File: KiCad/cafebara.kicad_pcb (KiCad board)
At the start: 4 copper layers, 49 x 32 mm, 60 parts, among them J1 Micro_SD_Card_Det2, J2 USB_C_Receptacle_USB2.0_14P, J3 PROG, J4 Conn_01x19_MountingPin, J6 EDID, Q1 NMOS, SW1 SW_Push, U3 ATtiny1616-M, U4 M24C02-RMC, U5 BQ25895RTW

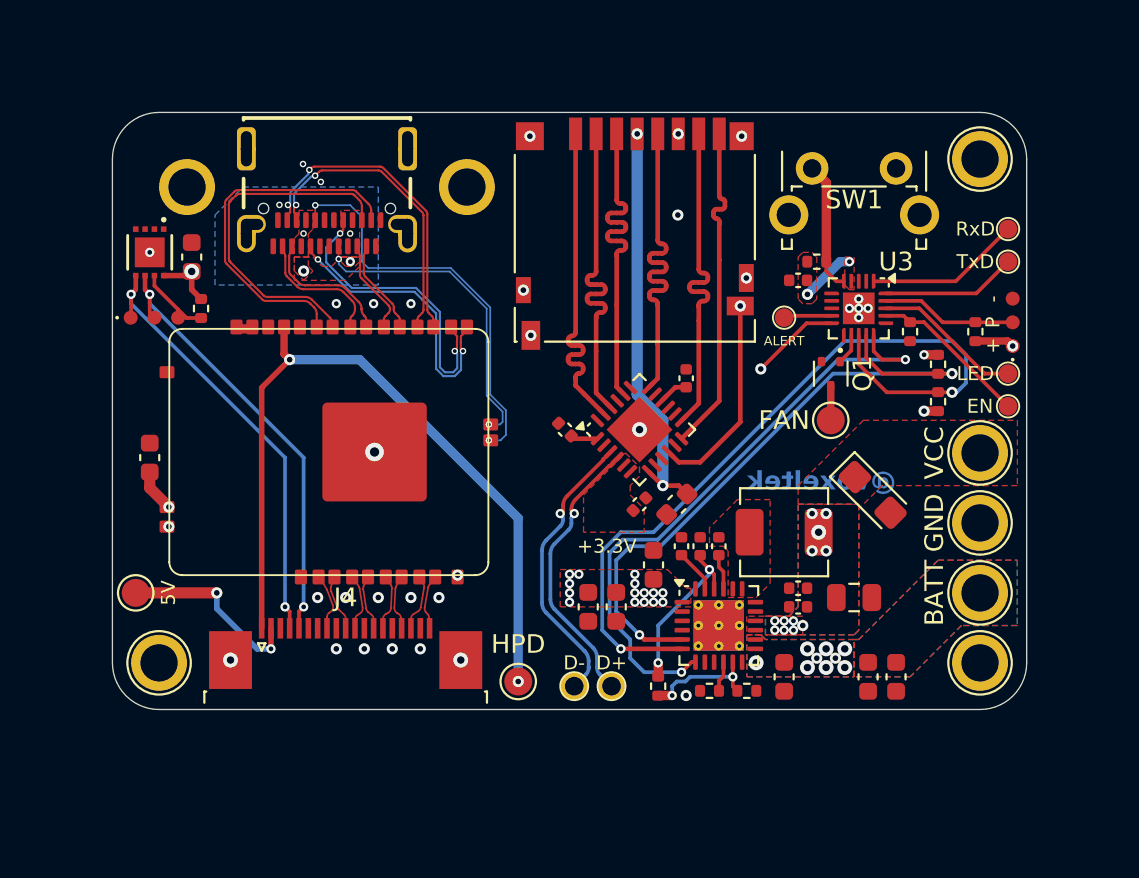
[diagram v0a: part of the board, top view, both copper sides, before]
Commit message: Begin change to new battery charge IC
TODO:
- complete transition
- add battery protection
- add fuel gauge?
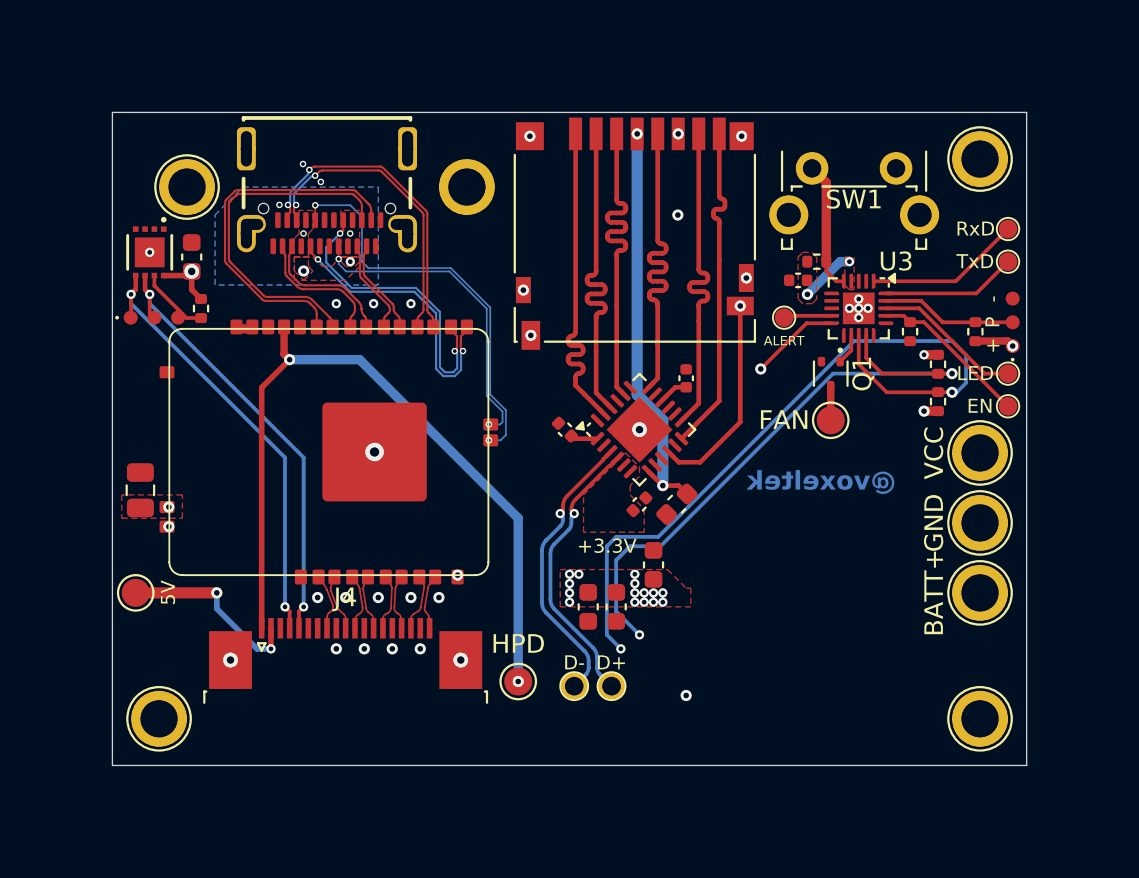
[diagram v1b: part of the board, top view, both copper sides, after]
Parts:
- removed C11: 22uF, Capacitor_SMD:C_0805_2012Metric
- removed C12: 47nF, Capacitor_SMD:C_0402_1005Metric
- removed C13, C16, C20: 10uF, Capacitor_SMD:C_0603_1608Metric
- removed C14: 4.7uF, Capacitor_SMD:C_0402_1005Metric
- removed C17, C18, C8: 22uF, Capacitor_SMD:C_0402_1005Metric
- removed C19: 100uF, Capacitor_Tantalum_SMD:CP_EIA-3216-10_Kemet-I
- removed L1: 3.3uH, Inductor_SMD:L_APV_APH0420
- removed R6: 260, Resistor_SMD:R_0402_1005Metric
- removed R7: 5.23k, Resistor_SMD:R_0402_1005Metric
- removed R8: 30.1k, Resistor_SMD:R_0402_1005Metric
- removed U5: BQ25895RTW, Package_DFN_QFN:Texas_RTW_WQFN-24-1EP_4x4mm_P0.5mm_EP2.7x2.7mm_ThermalVias
- C1: footprint Capacitor_SMD:C_0603_1608Metric -> Capacitor_SMD:C_0805_2012Metric
- TP5: value BATT -> BATT+
- moved H1 3.00 mm to (68.2, 74.0)
- moved H3 3.00 mm to (112.2, 74.0), turned to 90 degrees
- moved C1 1.82 mm to (67.2, 61.8)
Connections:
- TP5 pad 1: /BATT -> /BATT+
- U3 pad 15: ~{BQ_INT} -> unconnected-(U3-PC0-Pad15)
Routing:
- net ~{BQ_INT}: track 33.0 -> 0.00 mm, vias 2 -> 0
- net Net-(U5-REGN): track 9.00 -> 0.00 mm, vias 2 -> 0
- net Net-(U5-TS): track 6.33 -> 0.00 mm, vias 2 -> 0
- net SDA: track 43.1 -> 39.6 mm
- net SCL: track 35.2 -> 32.8 mm
- net Net-(U5-PMID): track 2.33 -> 0.00 mm
- net VBUS: track 20.1 -> 17.8 mm
- net Net-(U5-BTST): track 1.91 -> 0.00 mm
- net Net-(U5-ILIM): track 1.64 -> 0.00 mm
- net VCC: vias 17 -> 5
- net /BATT: vias 9 -> 0
- removed copper zone on B.Cu, net /BATT
- removed copper zone on F.Cu, net /BATT
- removed copper zone on In2.Cu, net /BATT
- removed copper zone on F.Cu, net Net-(C12-Pad1)
- removed copper zone on B.Cu, net VCC
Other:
- board size 49 x 32 mm -> 49 x 35 mm

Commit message: More misc progress
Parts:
- added REF**: Vishay_PowerPAK_SC70-6L_Single, Package_TO_SOT_SMD:Vishay_PowerPAK_SC70-6L_Single, F.Cu at (138.2, 79.3)
- added REF**: Diodes_UDFN2020-6_Type-F, Package_DFN_QFN:Diodes_UDFN2020-6_Type-F, F.Cu at (134.7, 79.3)
- added REF**: Vishay_PowerPAK_1212-8_Single, Package_SO:Vishay_PowerPAK_1212-8_Single, F.Cu at (153.0, 74.0)

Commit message: More misc work
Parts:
- removed the REF** at (138.2, 79.3)
- removed the REF** at (134.7, 79.3)
- removed the REF** at (153.0, 74.0)
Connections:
- net /BATT+ renamed /BMS/BATT+

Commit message: More work for BMS portion
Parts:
- added C11: 100uF, Capacitor_Tantalum_SMD:CP_EIA-3216-10_Kemet-I, F.Cu at (109.1, 93.2)
- added C12: 47nF, Capacitor_SMD:C_0402_1005Metric, F.Cu at (104.0, 65.5)
- added C13: 47nF, Capacitor_SMD:C_0402_1005Metric, F.Cu at (104.0, 107.5)
- added C14: 10nF, Capacitor_SMD:C_0402_1005Metric, F.Cu at (104.0, 109.5)
- added C16: 10nF, Capacitor_SMD:C_0402_1005Metric, F.Cu at (104.0, 111.5)
- added C17: 22uF, Capacitor_SMD:C_0402_1005Metric, F.Cu at (104.0, 113.5)
- added C18: 22uF, Capacitor_SMD:C_0402_1005Metric, F.Cu at (104.0, 115.4)
- added C19: 100uF, Capacitor_Tantalum_SMD:CP_EIA-3216-10_Kemet-I, F.Cu at (109.1, 96.4)
- added C20: 1nF, Capacitor_SMD:C_0402_1005Metric, F.Cu at (106.8, 103.6)
- added C21: 33nF, Capacitor_SMD:C_0402_1005Metric, F.Cu at (106.8, 105.6)
- added C22: 33nF, Capacitor_SMD:C_0402_1005Metric, F.Cu at (106.8, 107.5)
- added C23: 0.1uF, Capacitor_SMD:C_0402_1005Metric, F.Cu at (106.8, 109.5)
- added C24: 0.1uF, Capacitor_SMD:C_0402_1005Metric, F.Cu at (106.8, 111.5)
- added C25: 1uF, Capacitor_SMD:C_0402_1005Metric, F.Cu at (106.8, 113.5)
- added C26: 10uF, Capacitor_SMD:C_0603_1608Metric, F.Cu at (113.9, 96.2)
- added C27: 10uF, Capacitor_SMD:C_0603_1608Metric, F.Cu at (113.9, 98.7)
- added C28: 3.3uF, Capacitor_SMD:C_0402_1005Metric, F.Cu at (106.8, 115.4)
- added C29: 1uF, Capacitor_SMD:C_0402_1005Metric, F.Cu at (109.7, 103.6)
- added C30: 100pF, Capacitor_SMD:C_0402_1005Metric, F.Cu at (109.7, 105.6)
- added C31: 100pF, Capacitor_SMD:C_0402_1005Metric, F.Cu at (109.7, 107.5)
- added C32: 33pF, Capacitor_SMD:C_0402_1005Metric, F.Cu at (109.7, 109.5)
- added C33: 4.7nF, Capacitor_SMD:C_0402_1005Metric, F.Cu at (109.7, 111.5)
- added C34: 15pF, Capacitor_SMD:C_0402_1005Metric, F.Cu at (109.7, 113.5)
- added C35: 680pF, Capacitor_SMD:C_0402_1005Metric, F.Cu at (109.7, 115.4)
- added C8: 1uF, Capacitor_SMD:C_0402_1005Metric, F.Cu at (104.0, 103.6)
- added L1: 4.7uH, Inductor_SMD:L_APV_APH0420, F.Cu at (106.0, 62.5)
- added Q10: DMT3006, Package_DFN_QFN:Diodes_UDFN2020-6_Type-F, F.Cu at (104.3, 100.9)
- added Q2: DMT3006, Package_DFN_QFN:Diodes_UDFN2020-6_Type-F, F.Cu at (96.0, 93.5)
- added Q3: DMT3006, Package_DFN_QFN:Diodes_UDFN2020-6_Type-F, F.Cu at (96.0, 97.2)
- added Q4: DMT3006, Package_DFN_QFN:Diodes_UDFN2020-6_Type-F, F.Cu at (96.0, 100.9)
- added Q5: DMT3006, Package_DFN_QFN:Diodes_UDFN2020-6_Type-F, F.Cu at (100.1, 93.5)
- added Q6: DMP1009, Package_DFN_QFN:Diodes_UDFN2020-6_Type-F, F.Cu at (100.1, 97.2)
- added Q7: DMT3006, Package_DFN_QFN:Diodes_UDFN2020-6_Type-F, F.Cu at (100.1, 100.9)
- added Q8: DMT3006, Package_DFN_QFN:Diodes_UDFN2020-6_Type-F, F.Cu at (104.3, 93.5)
- added Q9: DMT3006, Package_DFN_QFN:Diodes_UDFN2020-6_Type-F, F.Cu at (104.3, 97.2)
- added R10: 5m, Resistor_SMD:R_0805_2012Metric, F.Cu at (113.3, 116.2)
- added R11: 330, Resistor_SMD:R_0402_1005Metric, F.Cu at (95.2, 109.6)
- added R12: 100k, Resistor_SMD:R_0402_1005Metric, F.Cu at (95.2, 111.6)
- added R13: 100k, Resistor_SMD:R_0402_1005Metric, F.Cu at (95.2, 113.6)
- added R14: 2.2k, Resistor_SMD:R_0402_1005Metric, F.Cu at (95.2, 115.6)
- added R15: 10m, Resistor_SMD:R_1206_3216Metric_Pad1.30x1.75mm_HandSolder, F.Cu at (114.9, 93.3)
- added R16: 10, Resistor_SMD:R_0402_1005Metric, F.Cu at (98.2, 103.6)
- added R17: 10, Resistor_SMD:R_0402_1005Metric, F.Cu at (98.2, 105.6)
- added R18: 10, Resistor_SMD:R_0402_1005Metric, F.Cu at (98.2, 107.6)
- added R19: 380k, Resistor_SMD:R_0402_1005Metric, F.Cu at (98.2, 109.6)
- added R20: 220k, Resistor_SMD:R_0402_1005Metric, F.Cu at (98.2, 111.6)
- added R21: 191k, Resistor_SMD:R_0402_1005Metric, F.Cu at (98.2, 113.6)
- added R22: 30k, Resistor_SMD:R_0402_1005Metric, F.Cu at (98.2, 115.6)
- added R23: 40.2k, Resistor_SMD:R_0402_1005Metric, F.Cu at (101.1, 103.6)
- added R24: 15k, Resistor_SMD:R_0402_1005Metric, F.Cu at (101.1, 105.6)
- added R25: 750k, Resistor_SMD:R_0402_1005Metric, F.Cu at (101.1, 107.6)
- added R26: 250k, Resistor_SMD:R_0402_1005Metric, F.Cu at (101.1, 109.6)
- added R6: 2.2, Resistor_SMD:R_0402_1005Metric, F.Cu at (95.2, 103.6)
- added R7: 4.99, Resistor_SMD:R_0402_1005Metric, F.Cu at (95.2, 105.6)
- added R8: 4.99, Resistor_SMD:R_0402_1005Metric, F.Cu at (95.2, 107.6)
- added TP12: BATT-, TestPoint:TestPoint_Plated_Hole_D2.0mm, F.Cu at (108.5, 100.3)
- added U5: BQ25730RSN, Package_DFN_QFN:Texas_RSN_WQFN-32-1EP_4x4mm_P0.4mm_EP2.8x2.8mm_ThermalVias, F.Cu at (104.8, 69.0)
- added U6: BQ297xy, Package_SON:WSON-6_1.5x1.5mm_P0.5mm, F.Cu at (117.7, 96.7)
- moved H3 2.93 mm to (115.0, 75.0)
- moved TP13 2.85 mm to (116.5, 48.8)
- moved TP14 2.85 mm to (116.5, 47.0)
- moved H4 2.75 mm to (115.0, 44.0)
- moved J3 2.75 mm to (116.8, 52.8)
- moved R3 2.75 mm to (114.8, 53.2)
- moved TP10 2.75 mm to (116.5, 55.5)
- moved TP5 2.75 mm to (115.0, 67.2)
- moved TP8 2.75 mm to (115.0, 59.8)
- moved TP9 2.75 mm to (115.0, 63.5)
- moved TP3 2.75 mm to (116.5, 57.2)
- moved H1 1.00 mm to (68.2, 75.0)
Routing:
- net RxD: track 8.36 -> 11.4 mm
- net TxD: track 7.25 -> 10.3 mm
- net /PA0: track 7.28 -> 10.0 mm
- net /LED: track 8.00 -> 10.7 mm
- net EN: track 8.56 -> 11.3 mm
- net /BMS/HIDRV1: track 0.00 -> 0.76 mm, vias 0 -> 1
- net GND: vias 35 -> 34
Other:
- board size 49 x 35 mm -> 51.8 x 36 mm

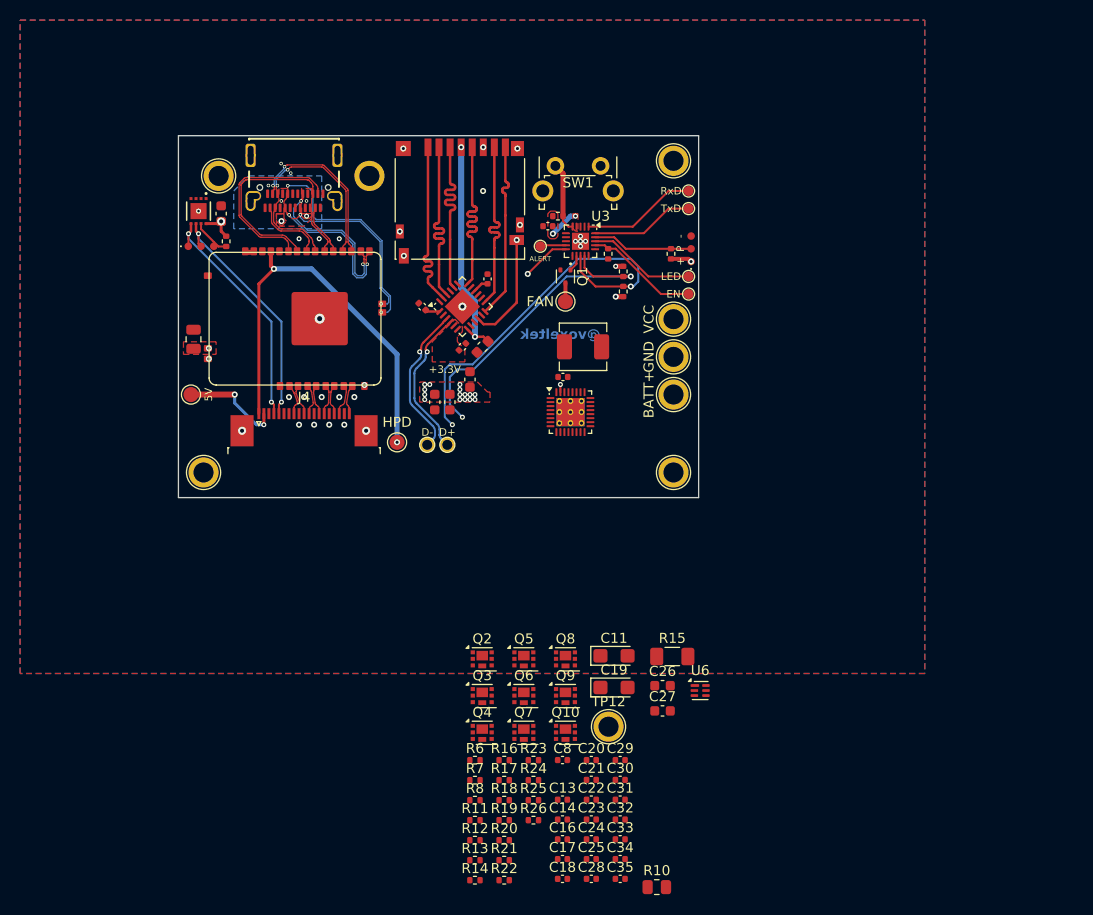
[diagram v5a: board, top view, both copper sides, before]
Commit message: Move to using 100W-Charging-PCB for battery charge
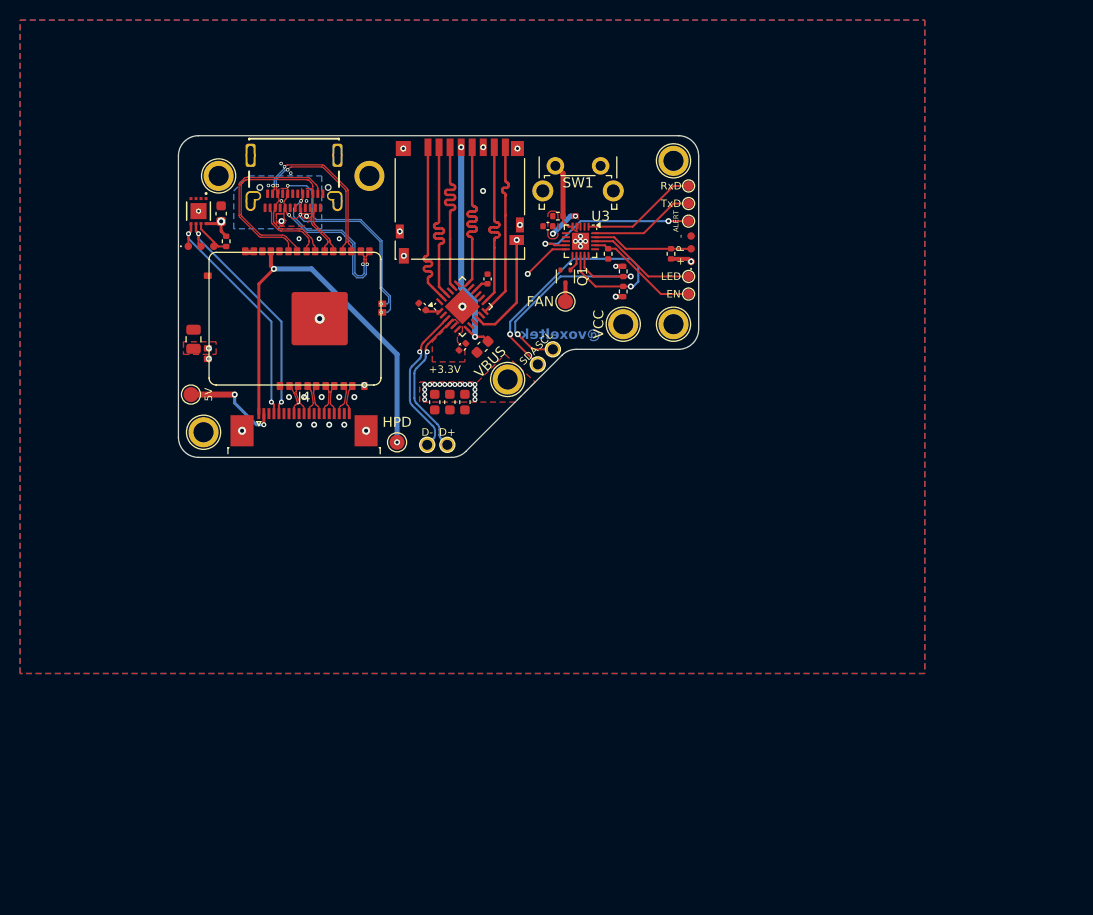
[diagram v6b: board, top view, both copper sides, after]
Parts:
- removed C11, C19: 100uF, Capacitor_Tantalum_SMD:CP_EIA-3216-10_Kemet-I
- removed C12, C13: 47nF, Capacitor_SMD:C_0402_1005Metric
- removed C14, C16: 10nF, Capacitor_SMD:C_0402_1005Metric
- removed C17, C18: 22uF, Capacitor_SMD:C_0402_1005Metric
- removed C20: 1nF, Capacitor_SMD:C_0402_1005Metric
- removed C21, C22: 33nF, Capacitor_SMD:C_0402_1005Metric
- removed C23, C24: 0.1uF, Capacitor_SMD:C_0402_1005Metric
- removed C25, C29, C8: 1uF, Capacitor_SMD:C_0402_1005Metric
- removed C26, C27: 10uF, Capacitor_SMD:C_0603_1608Metric
- removed C28: 3.3uF, Capacitor_SMD:C_0402_1005Metric
- removed C30, C31: 100pF, Capacitor_SMD:C_0402_1005Metric
- removed C32: 33pF, Capacitor_SMD:C_0402_1005Metric
- removed C33: 4.7nF, Capacitor_SMD:C_0402_1005Metric
- removed C34: 15pF, Capacitor_SMD:C_0402_1005Metric
- removed C35: 680pF, Capacitor_SMD:C_0402_1005Metric
- removed L1: 4.7uH, Inductor_SMD:L_APV_APH0420
- removed Q10, Q2, Q3, Q4, Q5, Q7, Q8, Q9: DMT3006, Package_DFN_QFN:Diodes_UDFN2020-6_Type-F
- removed Q6: DMP1009, Package_DFN_QFN:Diodes_UDFN2020-6_Type-F
- removed R10: 5m, Resistor_SMD:R_0805_2012Metric
- removed R11: 330, Resistor_SMD:R_0402_1005Metric
- removed R12, R13: 100k, Resistor_SMD:R_0402_1005Metric
- removed R14: 2.2k, Resistor_SMD:R_0402_1005Metric
- removed R15: 10m, Resistor_SMD:R_1206_3216Metric_Pad1.30x1.75mm_HandSolder
- removed R16, R17, R18: 10, Resistor_SMD:R_0402_1005Metric
- removed R19: 380k, Resistor_SMD:R_0402_1005Metric
- removed R20: 220k, Resistor_SMD:R_0402_1005Metric
- removed R21: 191k, Resistor_SMD:R_0402_1005Metric
- removed R22: 30k, Resistor_SMD:R_0402_1005Metric
- removed R23: 40.2k, Resistor_SMD:R_0402_1005Metric
- removed R24: 15k, Resistor_SMD:R_0402_1005Metric
- removed R25: 750k, Resistor_SMD:R_0402_1005Metric
- removed R26: 250k, Resistor_SMD:R_0402_1005Metric
- removed R6: 2.2, Resistor_SMD:R_0402_1005Metric
- removed R7, R8: 4.99, Resistor_SMD:R_0402_1005Metric
- removed TP12: BATT-, TestPoint:TestPoint_Plated_Hole_D2.0mm
- removed the TP5 at (115.0, 67.2)
- removed U5: BQ25730RSN, Package_DFN_QFN:Texas_RSN_WQFN-32-1EP_4x4mm_P0.4mm_EP2.8x2.8mm_ThermalVias
- removed U6: BQ297xy, Package_SON:WSON-6_1.5x1.5mm_P0.5mm
- added TP15: VBUS, TestPoint:TestPoint_Plated_Hole_D2.0mm, F.Cu at (98.5, 65.8)
- added TP8: SDA, cafebara:TestPoint_Hole_D1.5mm_Small, F.Cu at (101.5, 64.2)
- TP1, TP2: footprint cafebara:TestPoint_Pad_D1.0mm_Small -> cafebara:TestPoint_Hole_D1.5mm_Small
- TP9: value GND -> SCL; footprint TestPoint:TestPoint_Plated_Hole_D2.0mm -> cafebara:TestPoint_Hole_D1.5mm_Small
- moved TP7 15.0 mm to (116.5, 50.0), turned to -90 degrees
- moved H3 14.8 mm to (115.0, 60.2), turned to -90 degrees
- moved TP9 12.0 mm to (103.0, 62.8), turned to -135 degrees
- moved TP5 5.02 mm to (110.0, 60.2)
- moved H1 4.00 mm to (68.2, 71.0)
- moved C15 2.30 mm to (94.2, 68.0), turned to -90 degrees
- moved TP13 0.50 mm to (116.5, 48.2)
- moved TP14 0.50 mm to (116.5, 46.5)
- renumbered TP8 to TP5
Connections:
- TP9 pad 1: GND -> SCL
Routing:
- net ~{ALERT}: track 2.59 -> 17.3 mm, vias 0 -> 2
- net SDA: track 39.6 -> 30.7 mm
- net SCL: track 32.8 -> 25.0 mm
- net /BMS/HIDRV1: track 0.76 -> 0.00 mm, vias 1 -> 0
- net VBUS: vias 20 -> 22
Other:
- board size 51.8 x 36 mm -> 51.8 x 32 mm

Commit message: misc changes and improvements
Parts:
- added TP12: ~{SHIP}, cafebara:TestPoint_Pad_D1.0mm_Small, F.Cu at (112.5, 61.8)
- J6: value EDID -> EDID_PRG
- moved Q1 3.61 mm to (102.2, 58.5), turned to -45 degrees
- moved TP4 3.34 mm to (105.0, 61.2), turned to -90 degrees
- moved TP8 2.12 mm to (103.0, 62.8)
- moved TP9 2.12 mm to (101.5, 64.2)
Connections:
- U3 pad 15: unconnected-(U3-PC0-Pad15) -> ~{SHIP}
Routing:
- net VBUS: track 17.8 -> 2.57 mm
- net ~{SHIP}: track 0.00 -> 14.5 mm, vias 0 -> 2
- net SDA: track 30.7 -> 25.9 mm, vias 2 -> 1
- net FAN_PWM: track 1.65 -> 5.57 mm
- net Net-(Q1-D): track 1.85 -> 3.24 mm
- net SCL: track 25.0 -> 25.4 mm, vias 2 -> 1
